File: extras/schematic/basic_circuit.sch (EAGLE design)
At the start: 10 parts, among them M1 ARDUINO-PRO-MINI-3.3V, Y1 32.768kHz

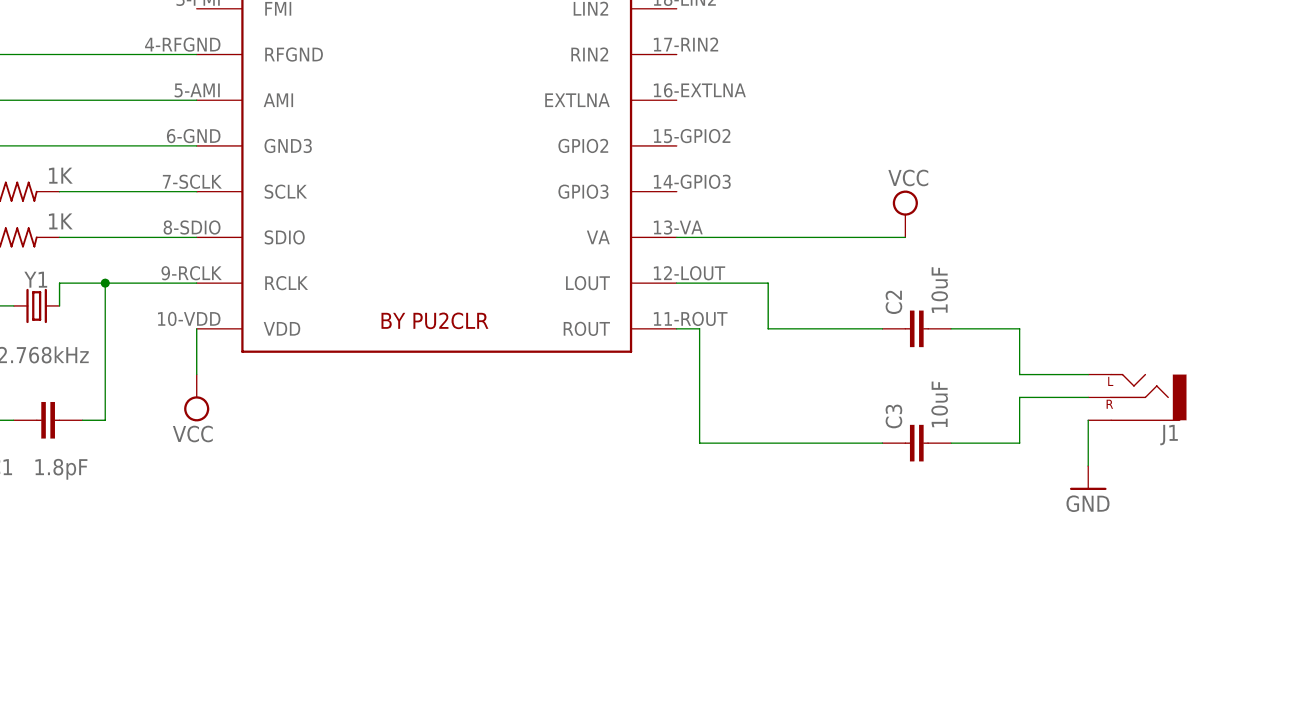
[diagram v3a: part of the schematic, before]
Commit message: BK1088 Arduino Library
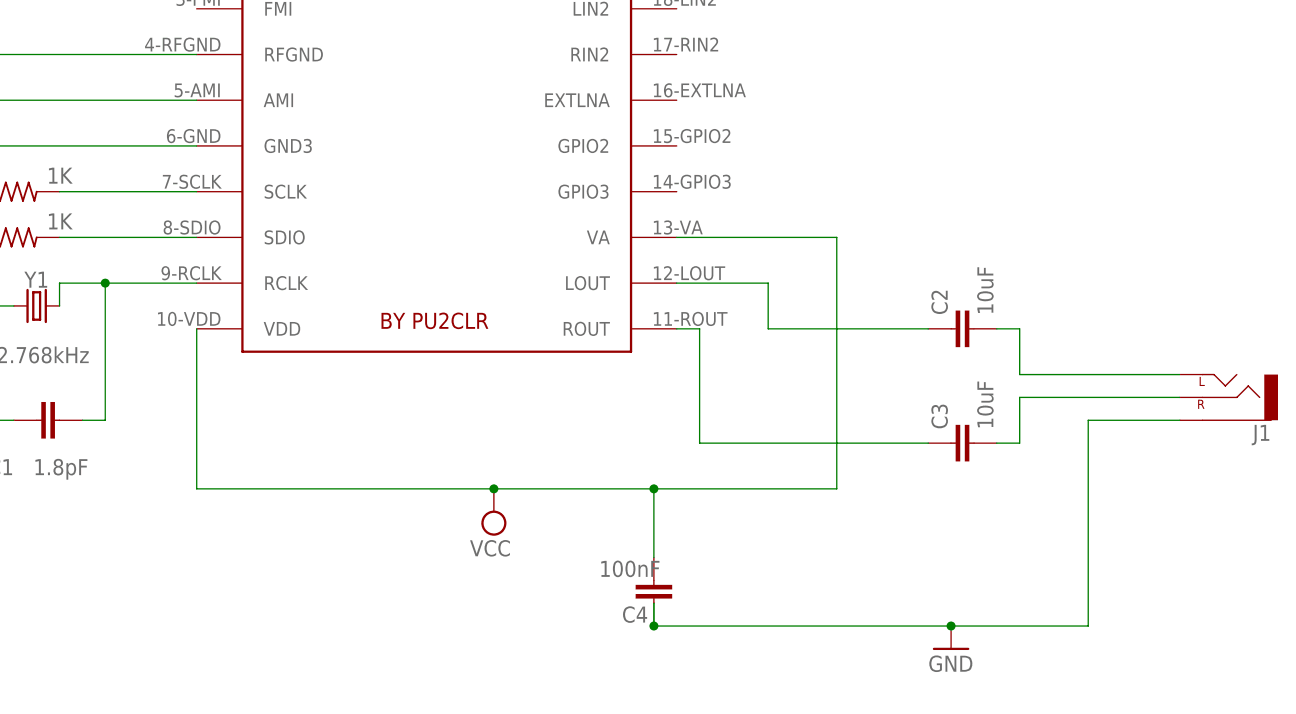
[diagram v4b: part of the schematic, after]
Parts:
- added C4: 100nF, capacitor-wima:C5/3
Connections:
- net GND: now also C4.2
- net VCC: now also C4.1
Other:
- moved on the sheet: C2, C3, J1
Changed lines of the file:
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@@
 <?xml version="1.0" encoding="utf-8"?>
 <!DOCTYPE eagle SYSTEM "eagle.dtd">
-<eagle version="9.4.2">
+<eagle version="9.6.2">
 <drawing>
 <settings>
@@
 <part name="R2" library="Resistor" library_urn="urn:adsk.eagle:library:16378527" deviceset="R-US" device="AXIAL-7.2MM-PITCH" package3d_urn="urn:adsk.eagle:package:16378561/2" technology="_" value="1K"/>
 <part name="SUPPLY2" library="supply2" library_urn="urn:adsk.eagle:library:372" deviceset="VCC" device=""/>
-<part name="SUPPLY3" library="supply2" library_urn="urn:adsk.eagle:library:372" deviceset="VCC" device=""/>
 <part name="GND5" library="supply1" library_urn="urn:adsk.eagle:library:371" deviceset="GND" device=""/>
 <part name="GND4" library="supply1" library_urn="urn:adsk.eagle:library:371" deviceset="GND" device=""/>
@@
 <part name="C2" library="SparkFun-Capacitors" library_urn="urn:adsk.eagle:library:510" deviceset="10UF" device="-0603-6.3V-20%" package3d_urn="urn:adsk.eagle:package:37414/1" value="10uF"/>
 <part name="C3" library="SparkFun-Capacitors" library_urn="urn:adsk.eagle:library:510" deviceset="10UF" device="-0603-6.3V-20%" package3d_urn="urn:adsk.eagle:package:37414/1" value="10uF"/>
-<part name="GND6" library="supply1" library_urn="urn:adsk.eagle:library:371" deviceset="GND" device=""/>
 <part name="J1" library="SparkFun-Connectors" library_urn="urn:adsk.eagle:library:513" deviceset="AUDIO_JACK_2.5MM" device="SPECIAL_POGO_PINS" package3d_urn="urn:adsk.eagle:package:38005/1"/>
 <part name="SUPPLY1" library="supply2" library_urn="urn:adsk.eagle:library:372" deviceset="VCC" device=""/>
@@
 <part name="U$2" library="adafruit" library_urn="urn:adsk.eagle:library:420" deviceset="FB" device="" package3d_urn="urn:adsk.eagle:package:6240653/1"/>
 <part name="GND8" library="supply1" library_urn="urn:adsk.eagle:library:371" deviceset="GND" device=""/>
+<part name="GND9" library="supply1" library_urn="urn:adsk.eagle:library:371" deviceset="GND" device=""/>
+<part name="C4" library="capacitor-wima" library_urn="urn:adsk.eagle:library:116" deviceset="C" device="5/3" package3d_urn="urn:adsk.eagle:package:5433/1" value="100nF"/>
 </parts>
 <sheets>
@@
 <attribute name="VALUE" x="33.02" y="42.418" size="1.778" layer="96" align="center"/>
 </instance>
-<instance part="SUPPLY2" gate="G$1" x="48.26" y="22.86" smashed="yes" rot="R180">
-<attribute name="VALUE" x="50.165" y="19.685" size="1.778" layer="96" rot="R180"/>
-</instance>
-<instance part="SUPPLY3" gate="G$1" x="127" y="43.18" smashed="yes">
-<attribute name="VALUE" x="125.095" y="46.355" size="1.778" layer="96"/>
+<instance part="SUPPLY2" gate="G$1" x="81.28" y="10.16" smashed="yes" rot="R180">
+<attribute name="VALUE" x="83.185" y="6.985" size="1.778" layer="96" rot="R180"/>
 </instance>
 <instance part="GND5" gate="1" x="-66.04" y="30.48" smashed="yes" rot="R180">
@@
 <attribute name="VALUE" x="30.48" y="28.448" size="1.778" layer="96" font="vector" align="top-center"/>
 </instance>
-<instance part="C2" gate="G$1" x="129.54" y="30.48" smashed="yes" rot="R90">
-<attribute name="NAME" x="126.619" y="32.004" size="1.778" layer="95" font="vector" rot="R90"/>
-<attribute name="VALUE" x="131.699" y="32.004" size="1.778" layer="96" font="vector" rot="R90"/>
-</instance>
-<instance part="C3" gate="G$1" x="129.54" y="17.78" smashed="yes" rot="R90">
-<attribute name="NAME" x="126.619" y="19.304" size="1.778" layer="95" font="vector" rot="R90"/>
-<attribute name="VALUE" x="131.699" y="19.304" size="1.778" layer="96" font="vector" rot="R90"/>
-</instance>
-<instance part="GND6" gate="1" x="147.32" y="12.7" smashed="yes">
-<attribute name="VALUE" x="144.78" y="10.16" size="1.778" layer="96"/>
-</instance>
-<instance part="J1" gate="G$1" x="152.4" y="22.86" smashed="yes" rot="R180">
-<attribute name="NAME" x="157.48" y="19.812" size="1.778" layer="95" font="vector" rot="R180"/>
-<attribute name="VALUE" x="157.48" y="27.94" size="1.778" layer="96" font="vector" rot="R180"/>
+<instance part="C2" gate="G$1" x="134.62" y="30.48" smashed="yes" rot="R90">
+<attribute name="NAME" x="131.699" y="32.004" size="1.778" layer="95" font="vector" rot="R90"/>
+<attribute name="VALUE" x="136.779" y="32.004" size="1.778" layer="96" font="vector" rot="R90"/>
+</instance>
+<instance part="C3" gate="G$1" x="134.62" y="17.78" smashed="yes" rot="R90">
+<attribute name="NAME" x="131.699" y="19.304" size="1.778" layer="95" font="vector" rot="R90"/>
+<attribute name="VALUE" x="136.779" y="19.304" size="1.778" layer="96" font="vector" rot="R90"/>
+</instance>
+<instance part="J1" gate="G$1" x="162.56" y="22.86" smashed="yes" rot="R180">
+<attribute name="NAME" x="167.64" y="19.812" size="1.778" layer="95" font="vector" rot="R180"/>
+<attribute name="VALUE" x="167.64" y="27.94" size="1.778" layer="96" font="vector" rot="R180"/>
 </instance>
 <instance part="SUPPLY1" gate="G$1" x="12.7" y="25.4" smashed="yes" rot="R270">
@@
 <instance part="GND8" gate="1" x="-22.86" y="93.98" smashed="yes" rot="R180">
 <attribute name="VALUE" x="-20.32" y="96.52" size="1.778" layer="96" rot="R180"/>
+</instance>
+<instance part="GND9" gate="1" x="132.08" y="-5.08" smashed="yes">
+<attribute name="VALUE" x="129.54" y="-7.62" size="1.778" layer="96"/>
+</instance>
+<instance part="C4" gate="G$1" x="99.06" y="2.54" smashed="yes">
+<attribute name="NAME" x="95.504" y="-2.159" size="1.778" layer="95"/>
+<attribute name="VALUE" x="92.964" y="2.921" size="1.778" layer="96"/>
 </instance>
 </instances>
@@
 </segment>
 <segment>
-<pinref part="J1" gate="G$1" pin="SLEEVE"/>
-<pinref part="GND6" gate="1" pin="GND"/>
-<wire x1="147.32" y1="20.32" x2="147.32" y2="15.24" width="0.1524" layer="91"/>
-</segment>
-<segment>
 <pinref part="GND7" gate="1" pin="GND"/>
 <pinref part="M1" gate="G$1" pin="GND.2"/>
@@
 <wire x1="-22.86" y1="86.36" x2="-22.86" y2="91.44" width="0.1524" layer="91"/>
 </segment>
+<segment>
+<pinref part="J1" gate="G$1" pin="SLEEVE"/>
+<wire x1="157.48" y1="20.32" x2="147.32" y2="20.32" width="0.1524" layer="91"/>
+<wire x1="147.32" y1="20.32" x2="147.32" y2="-2.54" width="0.1524" layer="91"/>
+<pinref part="GND9" gate="1" pin="GND"/>
+<wire x1="147.32" y1="-2.54" x2="132.08" y2="-2.54" width="0.1524" layer="91"/>
+<pinref part="C4" gate="G$1" pin="2"/>
+<wire x1="99.06" y1="-2.54" x2="132.08" y2="-2.54" width="0.1524" layer="91"/>
+<junction x="132.08" y="-2.54"/>
+<wire x1="99.06" y1="-2.54" x2="99.06" y2="0" width="0.1524" layer="91"/>
+<junction x="99.06" y="-2.54"/>
+</segment>
 </net>
 <net name="VCC" class="0">
-<segment>
-<pinref part="U$1" gate="G$1" pin="VA"/>
-<pinref part="SUPPLY3" gate="G$1" pin="VCC"/>
-<wire x1="101.6" y1="40.64" x2="127" y2="40.64" width="0.1524" layer="91"/>
-</segment>
-<segment>
-<pinref part="U$1" gate="G$1" pin="VDD"/>
-<pinref part="SUPPLY2" gate="G$1" pin="VCC"/>
-<wire x1="48.26" y1="30.48" x2="48.26" y2="25.4" width="0.1524" layer="91"/>
-</segment>
 <segment>
 <pinref part="SUPPLY1" gate="G$1" pin="VCC"/>
 <pinref part="M1" gate="G$1" pin="VCC"/>
 <wire x1="10.16" y1="25.4" x2="0" y2="25.4" width="0.1524" layer="91"/>
+</segment>
+<segment>
+<pinref part="U$1" gate="G$1" pin="VDD"/>
+<wire x1="48.26" y1="30.48" x2="48.26" y2="12.7" width="0.1524" layer="91"/>
+<pinref part="SUPPLY2" gate="G$1" pin="VCC"/>
+<wire x1="48.26" y1="12.7" x2="81.28" y2="12.7" width="0.1524" layer="91"/>
+<pinref part="U$1" gate="G$1" pin="VA"/>
+<wire x1="101.6" y1="40.64" x2="119.38" y2="40.64" width="0.1524" layer="91"/>
+<wire x1="119.38" y1="40.64" x2="119.38" y2="12.7" width="0.1524" layer="91"/>
+<wire x1="119.38" y1="12.7" x2="99.06" y2="12.7" width="0.1524" layer="91"/>
+<junction x="81.28" y="12.7"/>
+<pinref part="C4" gate="G$1" pin="1"/>
+<wire x1="99.06" y1="12.7" x2="81.28" y2="12.7" width="0.1524" layer="91"/>
+<wire x1="99.06" y1="5.08" x2="99.06" y2="12.7" width="0.1524" layer="91"/>
+<junction x="99.06" y="12.7"/>
 </segment>
 </net>
@@
 <wire x1="104.14" y1="30.48" x2="104.14" y2="17.78" width="0.1524" layer="91"/>
 <pinref part="C3" gate="G$1" pin="1"/>
-<wire x1="104.14" y1="17.78" x2="124.46" y2="17.78" width="0.1524" layer="91"/>
+<wire x1="104.14" y1="17.78" x2="129.54" y2="17.78" width="0.1524" layer="91"/>
 </segment>
 </net>
@@
 <wire x1="111.76" y1="35.56" x2="111.76" y2="30.48" width="0.1524" layer="91"/>
 <pinref part="C2" gate="G$1" pin="1"/>
-<wire x1="111.76" y1="30.48" x2="124.46" y2="30.48" width="0.1524" layer="91"/>
+<wire x1="111.76" y1="30.48" x2="129.54" y2="30.48" width="0.1524" layer="91"/>
 </segment>
 </net>
@@
 <segment>
 <pinref part="C3" gate="G$1" pin="2"/>
-<wire x1="132.08" y1="17.78" x2="139.7" y2="17.78" width="0.1524" layer="91"/>
+<wire x1="137.16" y1="17.78" x2="139.7" y2="17.78" width="0.1524" layer="91"/>
 <wire x1="139.7" y1="17.78" x2="139.7" y2="22.86" width="0.1524" layer="91"/>
 <pinref part="J1" gate="G$1" pin="RIGHT"/>
-<wire x1="139.7" y1="22.86" x2="147.32" y2="22.86" width="0.1524" layer="91"/>
+<wire x1="139.7" y1="22.86" x2="157.48" y2="22.86" width="0.1524" layer="91"/>
 </segment>
 </net>
@@
 <segment>
 <pinref part="C2" gate="G$1" pin="2"/>
-<wire x1="132.08" y1="30.48" x2="139.7" y2="30.48" width="0.1524" layer="91"/>
+<wire x1="137.16" y1="30.48" x2="139.7" y2="30.48" width="0.1524" layer="91"/>
 <wire x1="139.7" y1="30.48" x2="139.7" y2="25.4" width="0.1524" layer="91"/>
 <pinref part="J1" gate="G$1" pin="LEFT"/>
-<wire x1="139.7" y1="25.4" x2="147.32" y2="25.4" width="0.1524" layer="91"/>
-</segment>
-</net>
+<wire x1="139.7" y1="25.4" x2="157.48" y2="25.4" width="0.1524" layer="91"/>
+</segment>
+</net>
